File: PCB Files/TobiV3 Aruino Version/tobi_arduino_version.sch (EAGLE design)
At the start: 45 parts

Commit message: route motor leads with heavy traces
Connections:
- removed net M3_M4_EN: DRIVER2.STBY
- net M2_M3_EN: now also DRIVER2.STBY
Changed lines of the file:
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@@
-</segment>
-</net>
-<net name="M3_M4_EN" class="0">
-<segment>
-<pinref part="DRIVER2" gate="G$1" pin="STBY"/>
-<wire x1="160.02" y1="78.74" x2="162.56" y2="78.74" width="0.1524" layer="91"/>
-<label x="165.1" y="78.74" size="1.778" layer="95"/>
 </segment>
 </net>
@@
 <label x="63.5" y="111.76" size="1.778" layer="95"/>
 </segment>
-</net>
+<segment>
+<pinref part="DRIVER2" gate="G$1" pin="STBY"/>
+<wire x1="160.02" y1="78.74" x2="162.56" y2="78.74" width="0.1524" layer="91"/>
+<label x="165.1" y="78.74" size="1.778" layer="95"/>
+</segment>
+</net>

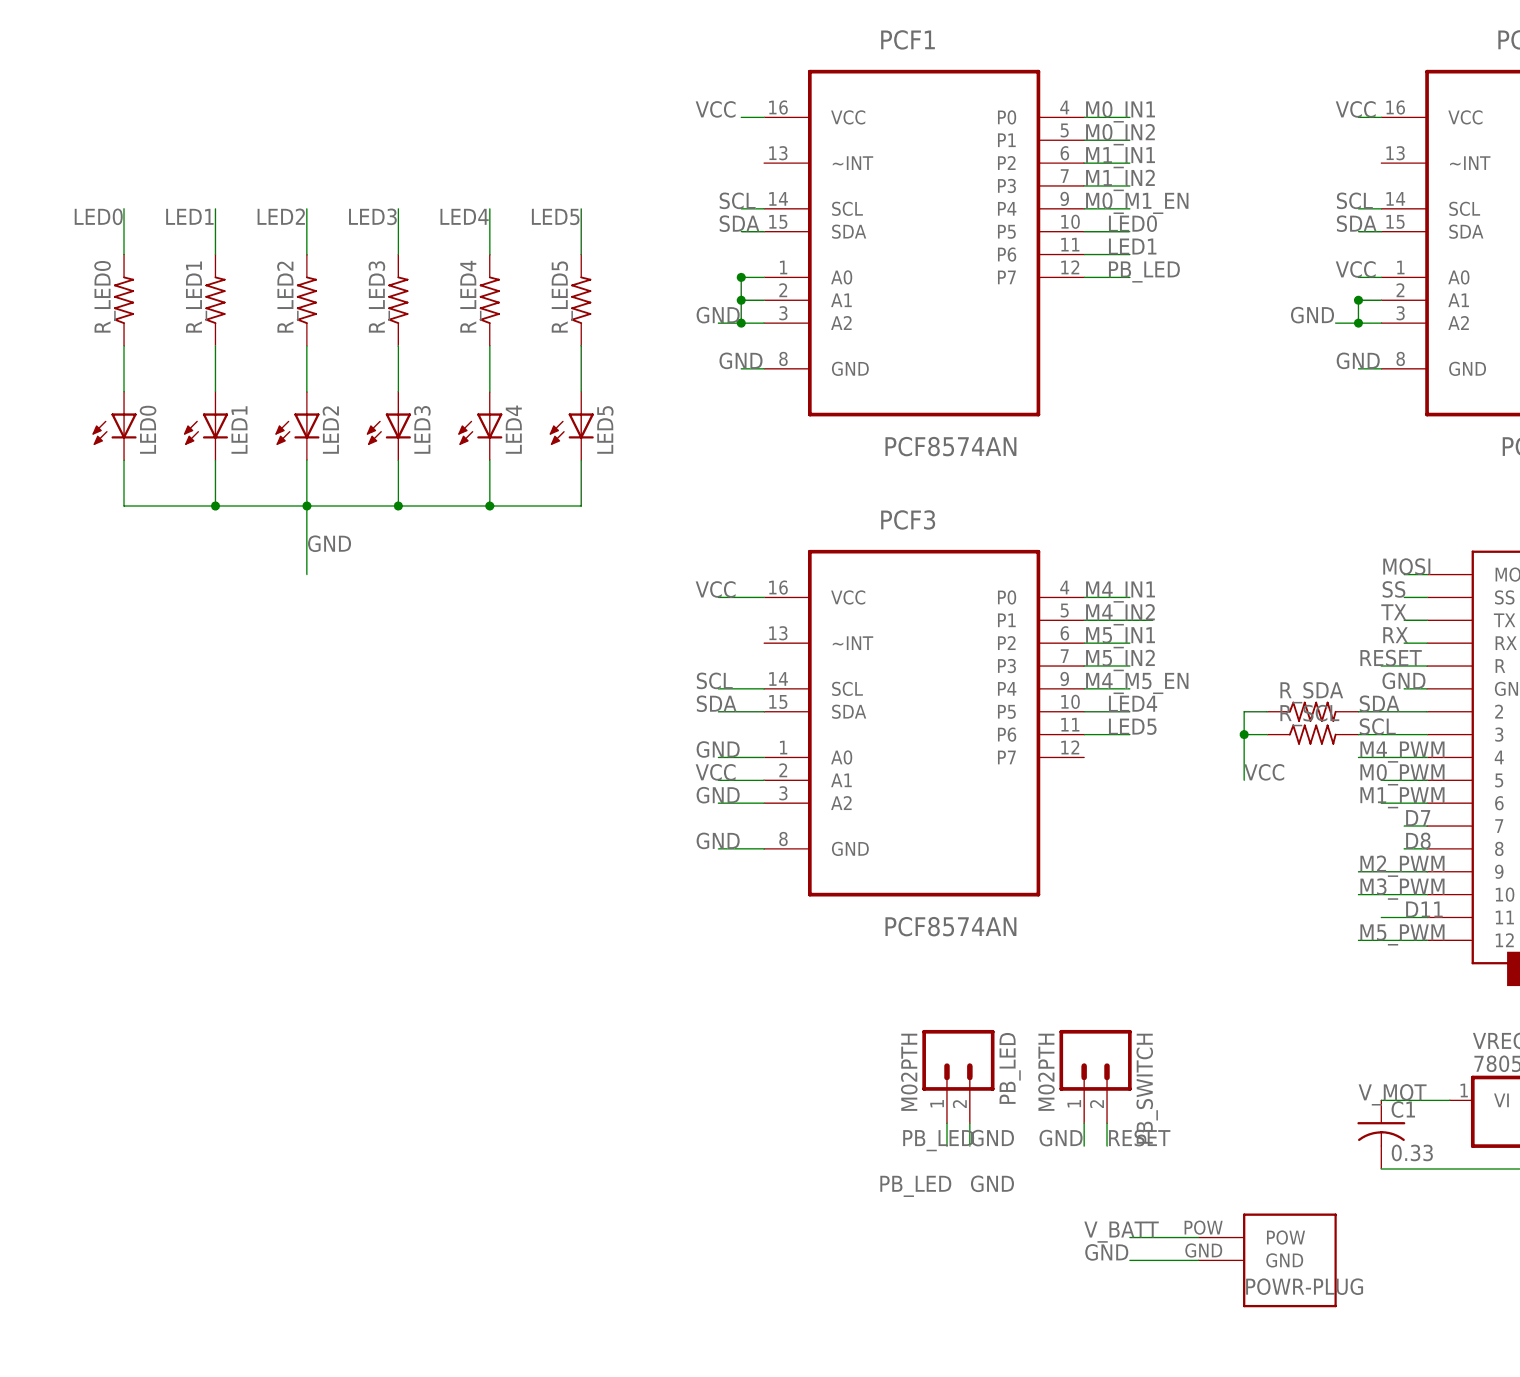
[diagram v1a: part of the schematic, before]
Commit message: fix LED hardware bugs
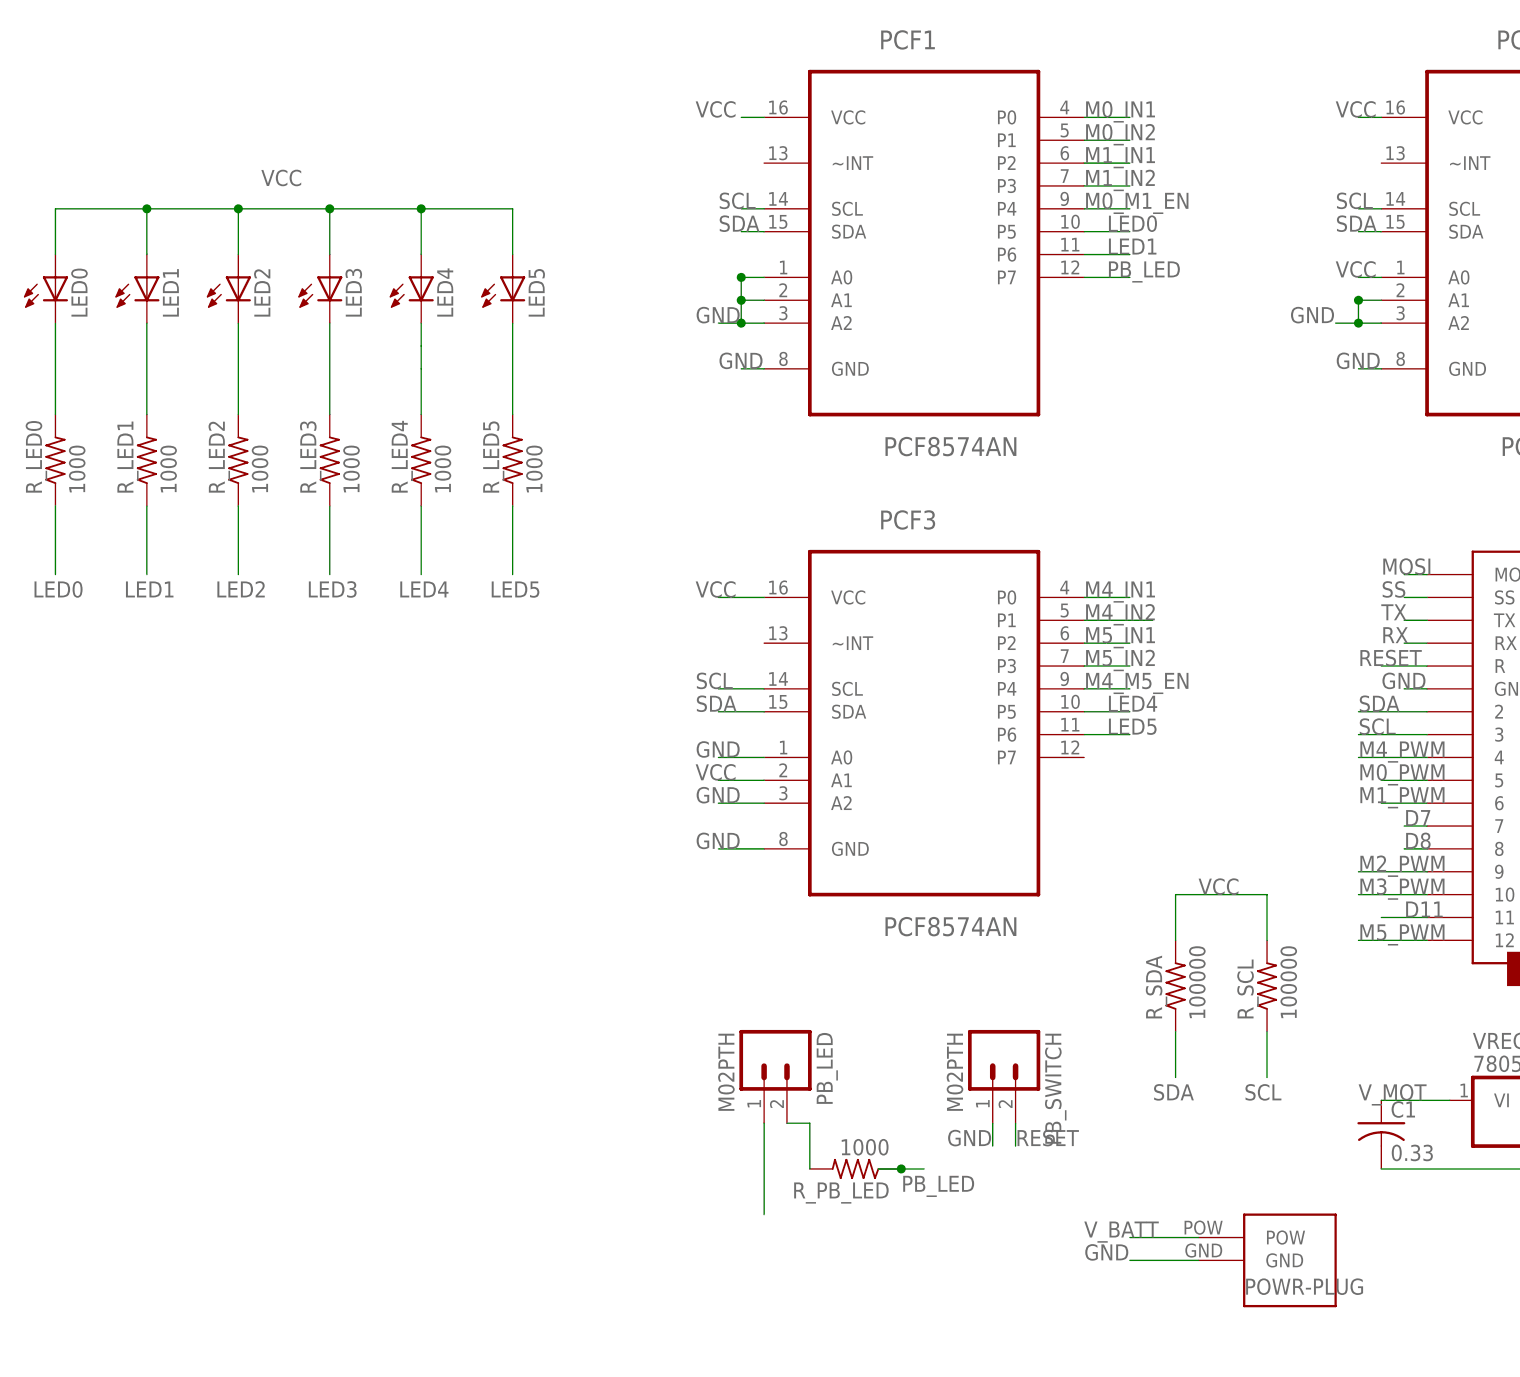
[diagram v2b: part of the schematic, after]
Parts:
- added R_PB_LED: 1000, resistor:R-US_0204/2V
- R_LED0, R_LED1, R_LED2, R_LED3, R_LED4, R_LED5: value (none) -> 1000
- R_SCL, R_SDA: value (none) -> 100000
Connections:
- removed net N$2: LED1.A, R_LED1.1
- removed net N$3: LED2.A, R_LED2.1
- removed net N$4: LED3.A, R_LED3.1
- removed net N$5: LED4.A, R_LED4.1
- removed net N$6: LED5.A, R_LED5.1
- net GND: no longer LED0.C, LED1.C, LED2.C, LED3.C, LED4.C, LED5.C, PB_LED.2
- net LED0: now also LED0.C, R_LED0.1
- net LED1: now also LED1.C, R_LED1.1
- net LED2: now also LED2.C, R_LED2.1
- net LED3: now also LED3.C, R_LED3.1
- net LED4: now also LED4.C, R_LED4.1
- net LED5: now also LED5.C, R_LED5.1
- net N$1: now also PB_LED.2, R_PB_LED.2; no longer LED0.A, R_LED0.1
- net PB_LED: now also R_PB_LED.1; no longer PB_LED.1
- net SCL: now also R_SCL.1; no longer R_SCL.2
- net SDA: now also R_SDA.1; no longer R_SDA.2
- net VCC: now also LED0.A, LED1.A, LED2.A, LED3.A, LED4.A, LED5.A, PB_LED.1, R_SCL.2, R_SDA.2; no longer R_SCL.1, R_SDA.1
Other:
- moved on the sheet: LED0, LED1, LED2, LED3, LED4, LED5, PB_LED, PB_SWITCH, R_LED0, R_LED1, R_LED2, R_LED3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
